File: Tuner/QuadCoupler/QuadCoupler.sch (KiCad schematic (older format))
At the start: 78 parts, among them J1 Conn_01x02, J10 Conn_01x02, J2 Conn_Coaxial, J21 Conn_01x01, J22 Conn_01x01, J23 Conn_01x01, J24 Conn_01x01, J3 Conn_Coaxial, J4 Conn_Coaxial, J5 Conn_Coaxial, J6 Conn_Coaxial, J7 Conn_01x02, J8 Conn_01x02, J9 Conn_01x02

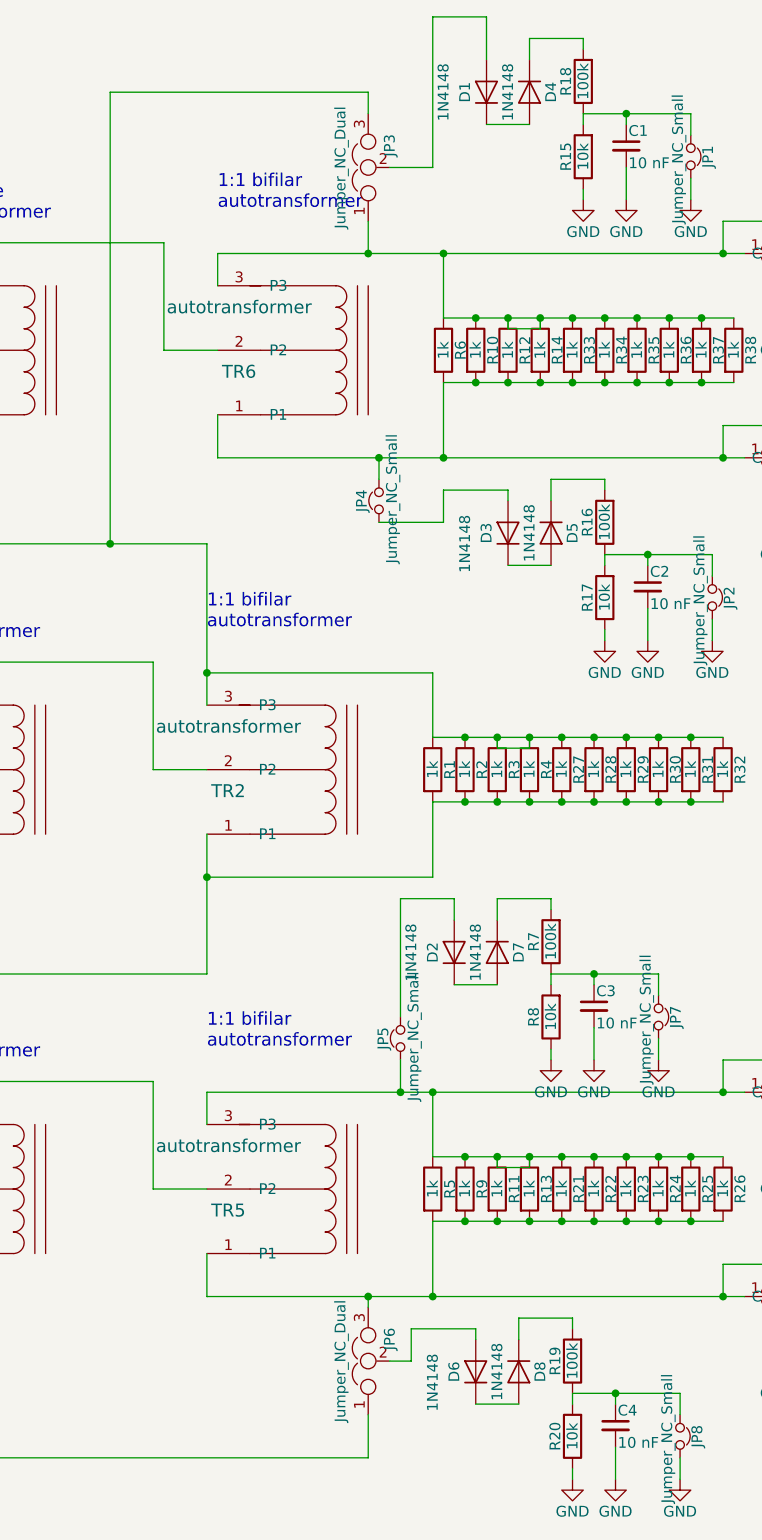
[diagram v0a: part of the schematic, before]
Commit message: Changed DelayLine to short out sections
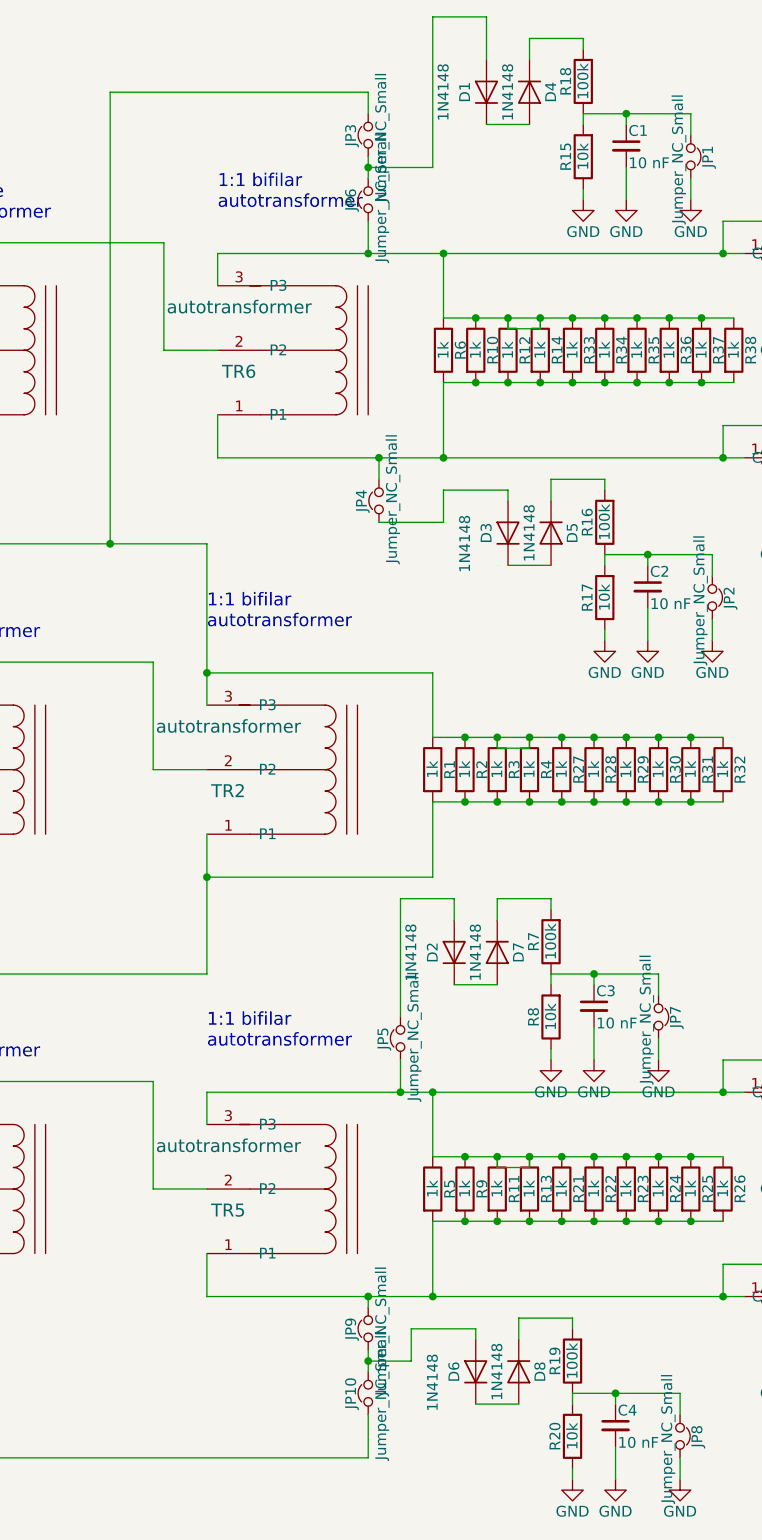
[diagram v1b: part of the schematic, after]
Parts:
- removed JP3, JP6: Jumper_NC_Dual, Pin_Headers:Pin_Header_Straight_1x03_Pitch2.54mm, symbol Jumper_NC_Dual
- added JP10, JP3, JP6, JP9: Jumper_NC_Small, Pin_Headers:Pin_Header_Straight_1x02_Pitch2.54mm, symbol Jumper_NC_Small
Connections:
- net at R1.2, R2.2, R27.2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: now also JP10.2
- net at R1.1, R2.1, R27.1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: now also JP3.1
- net at J2.1 (In), J7.2 (Pin_2), R10.1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: now also JP6.1
- net at J10.2 (Pin_2), J6.1 (In), R11.2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: now also JP9.1
- net at D1.2 (A): now also JP3.2, JP6.2
- net at D6.2 (A): now also JP10.1, JP9.2
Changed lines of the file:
@@
-$EndComp
-$Comp
-L Jumper_NC_Dual JP6
-U 1 1 5C72B745
-P 3850 6900
-F 0 "JP6" H 3900 6800 50  0000 L CNN
-F 1 "Jumper_NC_Dual" H 3850 7000 50  0000 C BNN
-F 2 "Pin_Headers:Pin_Header_Straight_1x03_Pitch2.54mm" H 3850 6900 50  0001 C CNN
-F 3 "" H 3850 6900 50  0001 C CNN
-	1    3850 6900
-	0    -1   -1   0
-$EndComp
-$Comp
-L Jumper_NC_Dual JP3
-U 1 1 5C72BF16
-P 3850 1350
-F 0 "JP3" H 3900 1250 50  0000 L CNN
-F 1 "Jumper_NC_Dual" H 3850 1450 50  0000 C BNN
-F 2 "Pin_Headers:Pin_Header_Straight_1x03_Pitch2.54mm" H 3850 1350 50  0001 C CNN
-F 3 "" H 3850 1350 50  0001 C CNN
-	1    3850 1350
-	0    -1   -1   0
 $EndComp
 $Comp
@@
 Connection ~ 3850 6600
 Wire Wire Line
-	3950 6900 4050 6900
+	3850 6900 4050 6900
 Wire Wire Line
 	4050 6900 4050 6750
@@
 Connection ~ 3850 1750
 Wire Wire Line
-	4150 1350 3950 1350
+	4150 1350 3850 1350
 Wire Wire Line
 	2650 3100 2650 1000
@@
 Text Notes 7700 7000 0    60   ~ 0
 QUAD POWER COUPLER\nBY DAN MARKS KW4TI\nCC-BY-SA 4.0
+$Comp
+L Jumper_NC_Small JP6
+U 1 1 5C7302D2
+P 3850 1500
+F 0 "JP6" H 3850 1580 50  0000 C CNN
+F 1 "Jumper_NC_Small" H 3860 1440 50  0000 C CNN
+F 2 "Pin_Headers:Pin_Header_Straight_1x02_Pitch2.54mm" H 3850 1500 50  0001 C CNN
+F 3 "" H 3850 1500 50  0001 C CNN
+	1    3850 1500
+	0    -1   -1   0
+$EndComp
+$Comp
+L Jumper_NC_Small JP3
+U 1 1 5C7303E0
+P 3850 1200
+F 0 "JP3" H 3850 1280 50  0000 C CNN
+F 1 "Jumper_NC_Small" H 3860 1140 50  0000 C CNN
+F 2 "Pin_Headers:Pin_Header_Straight_1x02_Pitch2.54mm" H 3850 1200 50  0001 C CNN
+F 3 "" H 3850 1200 50  0001 C CNN
+	1    3850 1200
+	0    -1   1    0
+$EndComp
+Wire Wire Line
+	3850 1400 3850 1300
+Connection ~ 3850 1350
+$Comp
+L Jumper_NC_Small JP9
+U 1 1 5C730A1B
+P 3850 6750
+F 0 "JP9" H 3850 6830 50  0000 C CNN
+F 1 "Jumper_NC_Small" H 3860 6690 50  0000 C CNN
+F 2 "Pin_Headers:Pin_Header_Straight_1x02_Pitch2.54mm" H 3850 6750 50  0001 C CNN
+F 3 "" H 3850 6750 50  0001 C CNN
+	1    3850 6750
+	0    -1   1    0
+$EndComp
+$Comp
+L Jumper_NC_Small JP10
+U 1 1 5C73132B
+P 3850 7050
+F 0 "JP10" H 3850 7130 50  0000 C CNN
+F 1 "Jumper_NC_Small" H 3860 6990 50  0000 C CNN
+F 2 "Pin_Headers:Pin_Header_Straight_1x02_Pitch2.54mm" H 3850 7050 50  0001 C CNN
+F 3 "" H 3850 7050 50  0001 C CNN
+	1    3850 7050
+	0    -1   1    0
+$EndComp
+Wire Wire Line
+	3850 6950 3850 6850
+Connection ~ 3850 6900
 $EndSCHEMATC

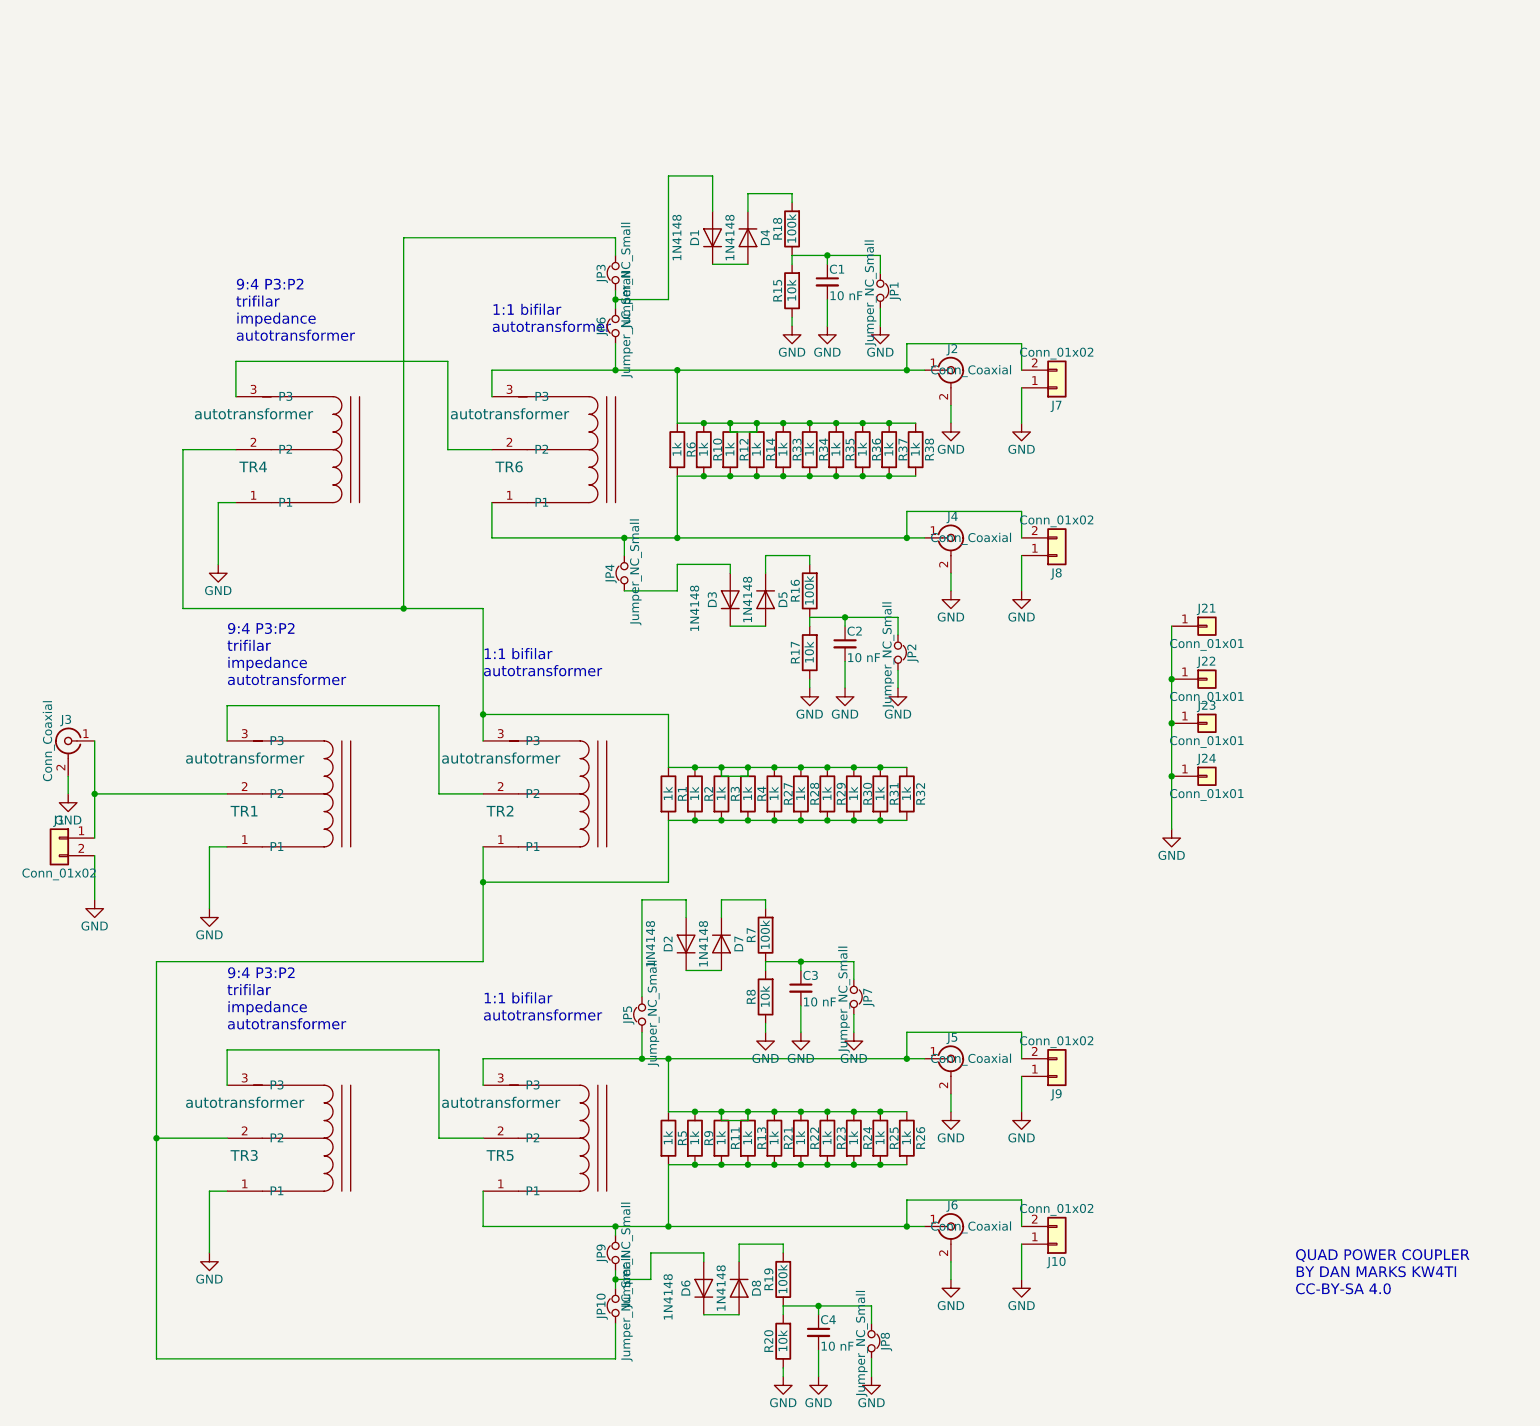
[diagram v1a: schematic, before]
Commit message: Added more instrumentation to TandemMatch, fixed grounding issue
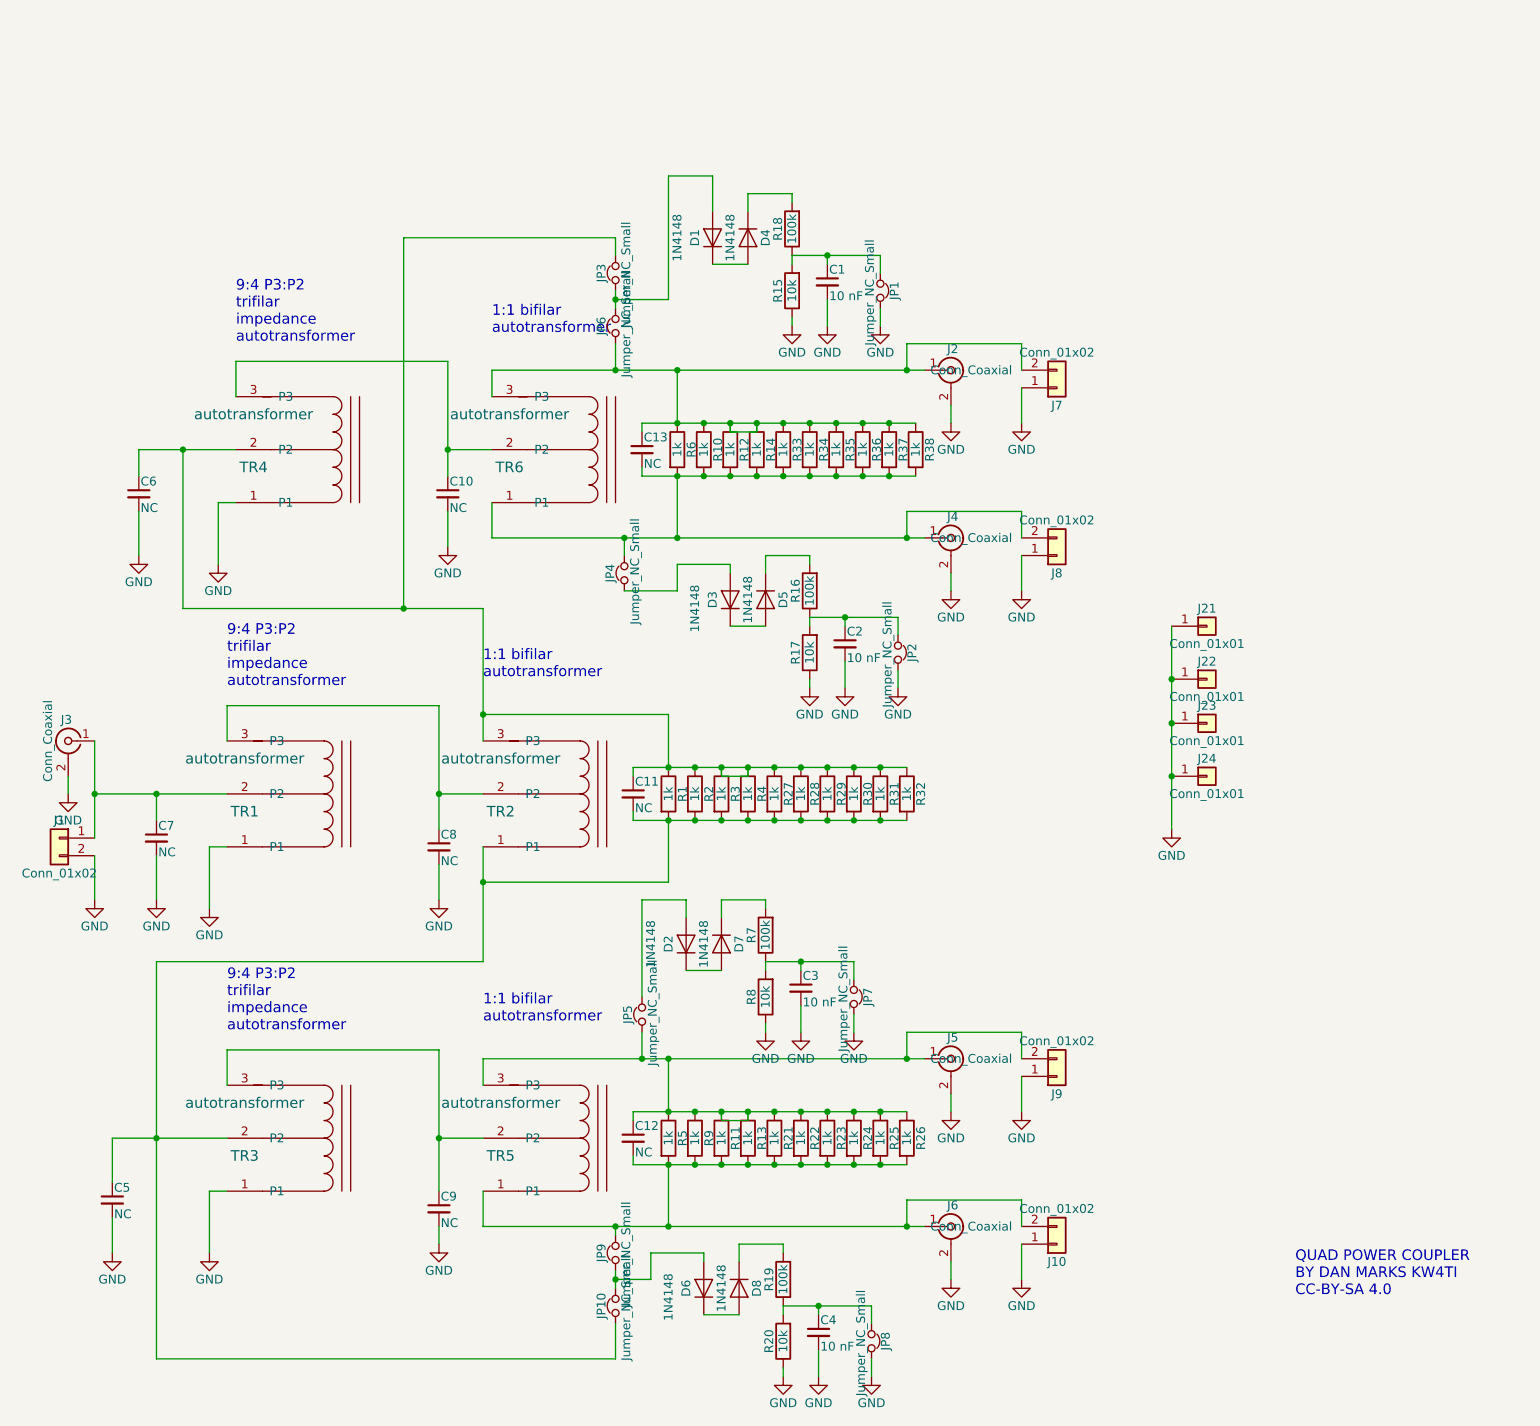
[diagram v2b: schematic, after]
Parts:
- added C10, C11, C12, C13, C5, C6, C7, C8, C9: NC, Capacitors_THT:C_Disc_D5.0mm_W2.5mm_P5.00mm, symbol C_Small
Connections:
- net GND: now also C10.2, C5.2, C6.2, C7.2, C8.2, C9.2
- net at J1.1 (Pin_1), J3.1 (In), TR1.2 (P2): now also C7.1
- net at TR1.3 (P3), TR2.2 (P2): now also C8.1
- net at JP10.2, R1.2, R2.2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: now also C11.2, C5.1
- net at JP3.1, R1.1, R2.1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: now also C11.1, C6.1
- net at TR4.3 (P3), TR6.2 (P2): now also C10.1
- net at J4.1 (In), J8.2 (Pin_2), JP4.2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: now also C13.2
- net at J2.1 (In), J7.2 (Pin_2), JP6.1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: now also C13.1
- net at TR3.3 (P3), TR5.2 (P2): now also C9.1
- net at J10.2 (Pin_2), J6.1 (In), JP9.1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: now also C12.2
- net at J5.1 (In), J9.2 (Pin_2), JP5.1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: now also C12.1
